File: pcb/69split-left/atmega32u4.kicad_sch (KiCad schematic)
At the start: 16 parts, among them J2 Conn_02x03_Odd_Even, SW1 SW_Push, U1 ATmega32U4-AU, Y1 Crystal

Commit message: Moved things around so it's less confusing.
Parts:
- renumbered C5 to C2, C6 to C3, C7 to C4, C8 to C5, C2 to C6, C3 to C7, C4 to C8, R8 to R6, R9 to R8, R6 to R9

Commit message: Started layout?
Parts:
- renumbered C6 to C1, C7 to C2, C8 to C3, C2 to C4, C3 to C5, C4 to C6, C5 to C7, J2 to J1, R5 to R1, R7 to R2, R6 to R3, R8 to R4, R9 to R5
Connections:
- net RESET: now also C4.1, R1.1, SW1.2, U1.13 (~{RESET})

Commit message: Continued layout.
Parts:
- removed R2, R3, R4: 330R, Resistor_SMD:R_0603_1608Metric_Pad0.98x0.95mm_HandSolder, symbol Device:R
- added C9: 1u, Capacitor_SMD:C_0603_1608Metric_Pad1.08x0.95mm_HandSolder, symbol Device:C_Small
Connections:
- net VBUS is gone; now on net VCC: U1.7 (VBUS)
- net GND: now also C9.2
- net GPIO_OUT_PB5: now also U1.29 (PB5)
- net GPIO_OUT_PB6: now also U1.30 (PB6)
- net GPIO_OUT_PB7: now also U1.12 (PB7)
- net VCC: now also C9.1
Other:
- moved on the sheet: C2

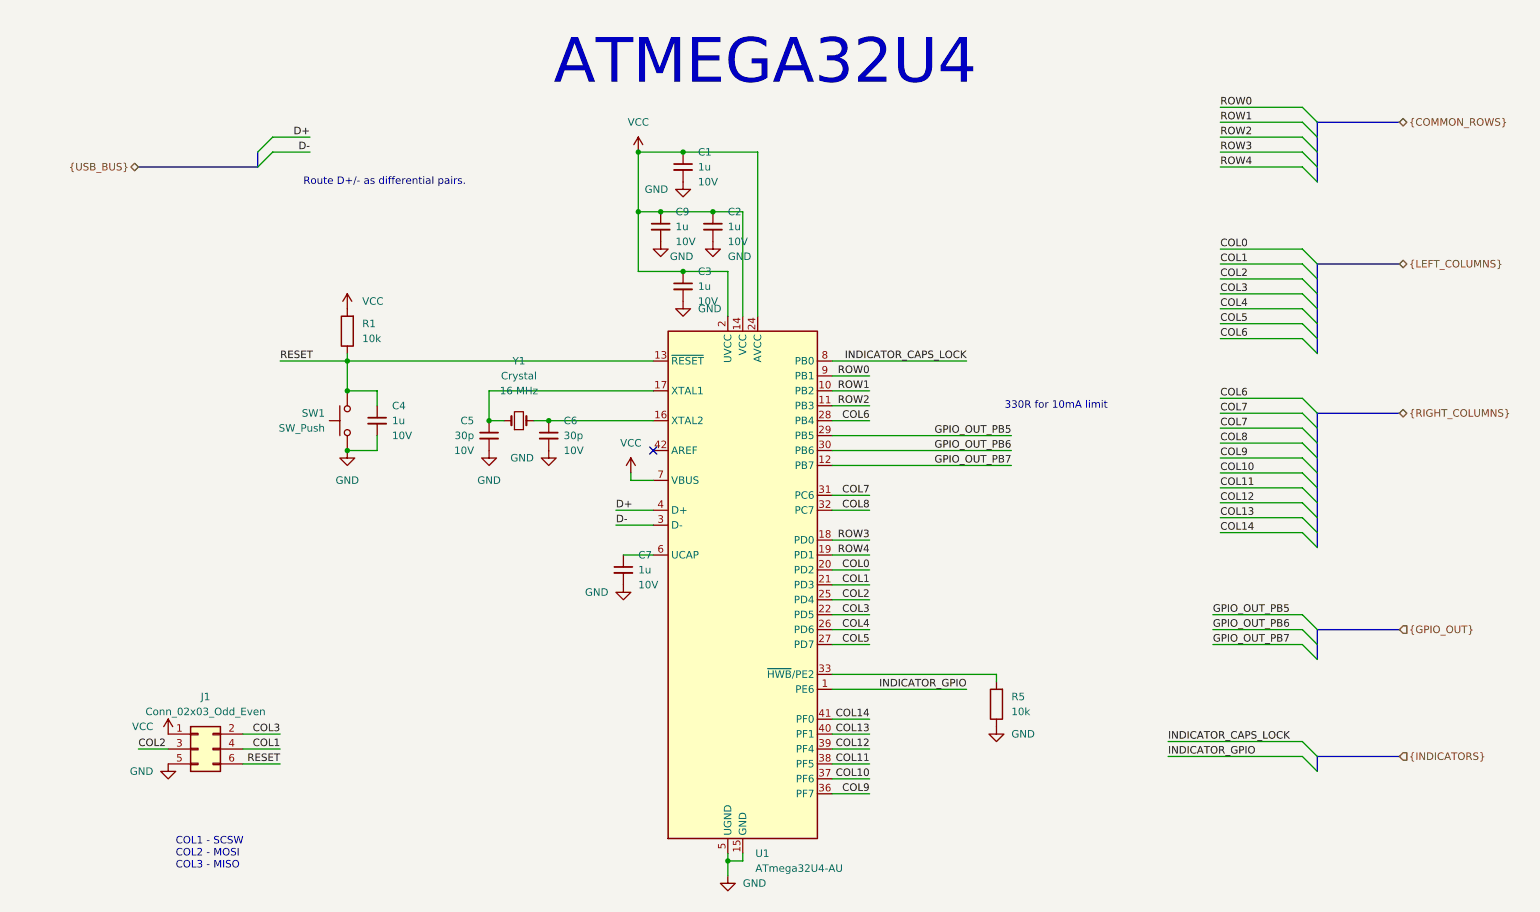
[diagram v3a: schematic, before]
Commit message: Practically finished the left side - need to make a footprint for the split USB connector. Some other schematic changes were made that I will not list. I should've made more commits between ths one and the previous one but it is what it is.
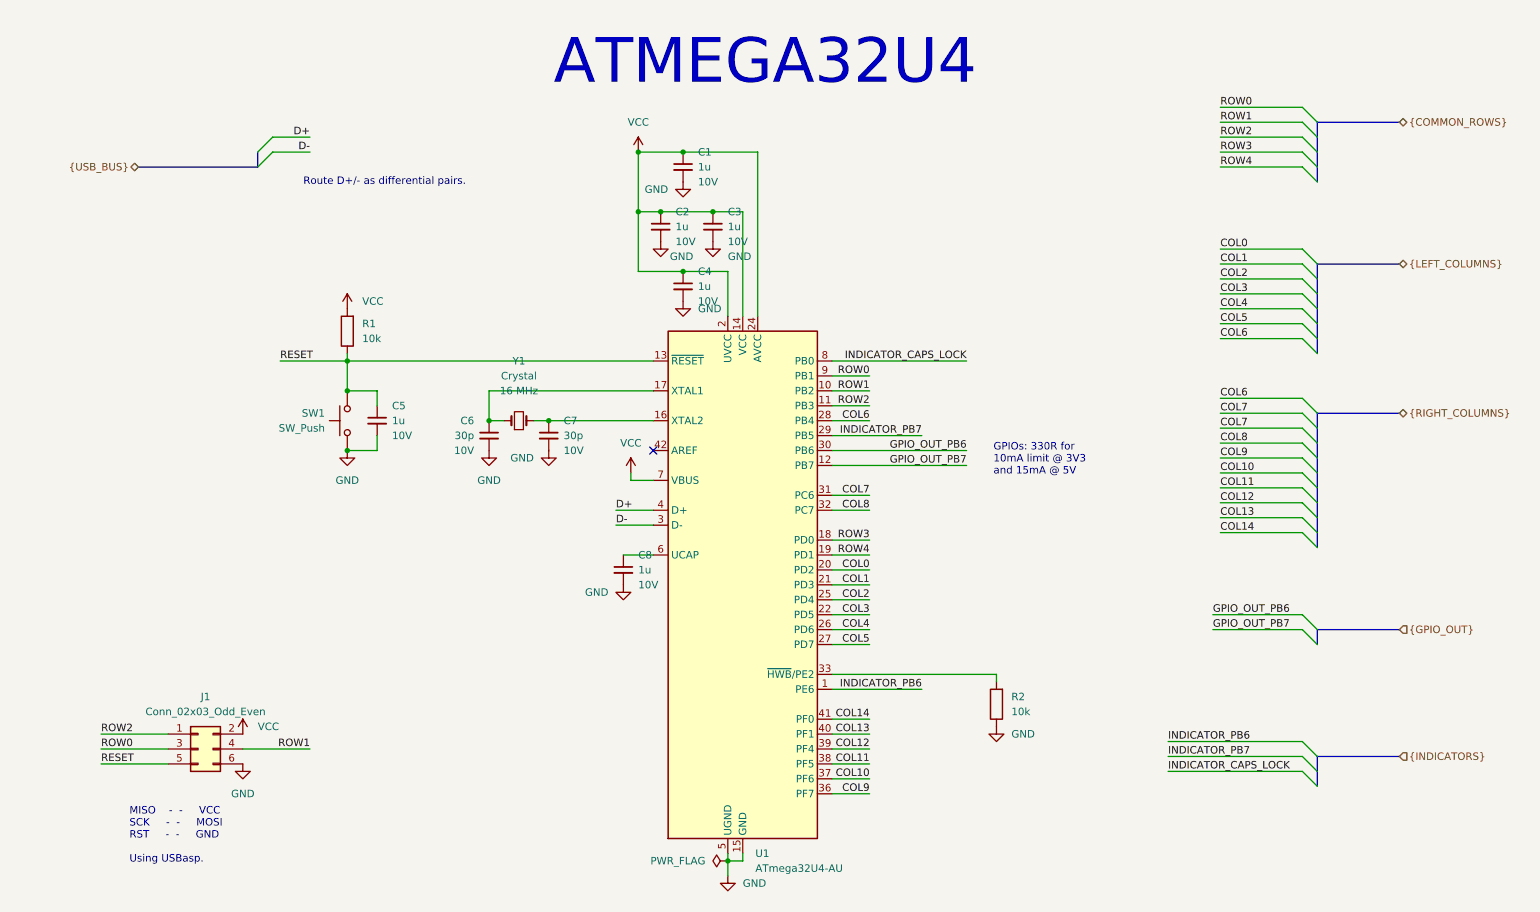
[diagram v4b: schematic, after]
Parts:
- renumbered C9 to C2, C2 to C3, C3 to C4, C4 to C5, C5 to C6, C6 to C7, C7 to C8, R5 to R2
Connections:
- net COL1: no longer J1.4 (Pin_4)
- net COL2: no longer J1.3 (Pin_3)
- net COL3: no longer J1.2 (Pin_2)
- net GND: now also J1.6 (Pin_6); no longer J1.5 (Pin_5)
- net RESET: now also J1.5 (Pin_5); no longer J1.6 (Pin_6)
- net ROW0: now also J1.3 (Pin_3)
- net ROW1: now also J1.4 (Pin_4)
- net ROW2: now also J1.1 (Pin_1)
- net VCC: now also J1.2 (Pin_2); no longer J1.1 (Pin_1)
- net GPIO_OUT_PB5 renamed INDICATOR_PB7
- net INDICATOR_GPIO renamed INDICATOR_PB6
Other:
- note added: "GPIOs: 330R for 10mA limit @ 3V3 and 15mA @ 5V"
- note added: "MISO - - VCC SCK - - MOSI RST - - GND Using USBasp."
- note removed: "330R for 10mA limit"
- note removed: "COL1 - SCSW COL2 - MOSI COL3 - MISO"

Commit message: Started changing things gain to use an I/O expander with I2C.
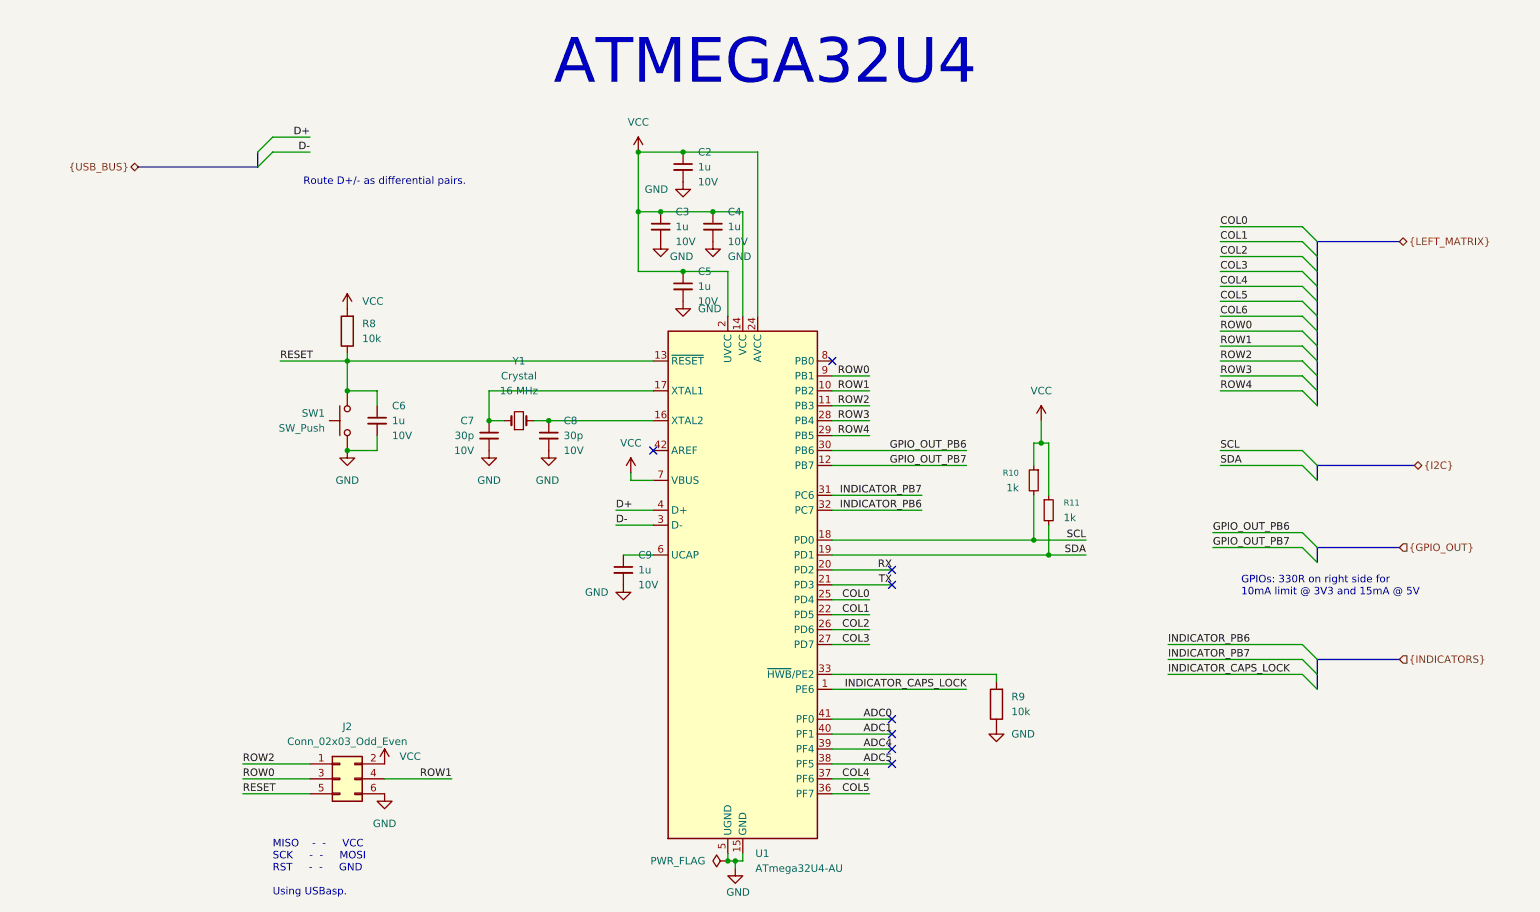
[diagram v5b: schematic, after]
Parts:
- added R10, R11: 1k, Resistor_SMD:R_0603_1608Metric_Pad0.98x0.95mm_HandSolder, symbol Device:R_Small
- renumbered C1 to C2, C2 to C3, C3 to C4, C4 to C5, C5 to C6, C6 to C7, C7 to C8, C8 to C9, J1 to J2, R1 to R8, R2 to R9
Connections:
- net COL10 is gone; now on net COL4: U1.37 (PF6)
- net COL7 is gone; now on net INDICATOR_PB7: U1.31 (PC6)
- net COL8 is gone; now on net INDICATOR_PB6: U1.32 (PC7)
- net COL9 is gone; now on net COL5: U1.36 (PF7)
- net COL0: now also U1.25 (PD4); no longer U1.20 (PD2)
- net COL1: now also U1.22 (PD5); no longer U1.21 (PD3)
- net COL2: now also U1.26 (PD6); no longer U1.25 (PD4)
- net COL3: now also U1.27 (PD7); no longer U1.22 (PD5)
- net COL4: no longer U1.26 (PD6)
- net COL5: no longer U1.27 (PD7)
- net COL6: no longer U1.28 (PB4)
- net INDICATOR_CAPS_LOCK: now also U1.1 (PE6); no longer U1.8 (PB0)
- net INDICATOR_PB6: no longer U1.1 (PE6)
- net INDICATOR_PB7: no longer U1.29 (PB5)
- net ROW3: now also U1.28 (PB4); no longer U1.18 (PD0)
- net ROW4: now also U1.29 (PB5); no longer U1.19 (PD1)
- net VCC: now also R10.1, R11.1
- net COL11 renamed ADC5
- net COL12 renamed ADC4
- net COL13 renamed ADC1
- net COL14 renamed ADC0
- new net RX: U1.20 (PD2)
- new net SCL: R10.2, U1.18 (PD0)
- new net SDA: R11.2, U1.19 (PD1)
- new net TX: U1.21 (PD3)
- no-connect marks 1 -> 8
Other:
- note added: "GPIOs: 330R on right side for 10mA limit @ 3V3 and 15mA @ 5V"
- note removed: "GPIOs: 330R for 10mA limit @ 3V3 and 15mA @ 5V"
- company: (none) -> Yiannis Michael
- title: 69SPLIT KEYBOARD -> 69SPLIT
- moved on the sheet: J2

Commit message: Finished left keyboard again...
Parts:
- R10, R11: now not fitted
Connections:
- net ADC5 is gone; now on net COL4: U1.38 (PF5)
- net COL4: no longer U1.37 (PF6)
- net COL5: now also U1.37 (PF6); no longer U1.36 (PF7)
- net COL6: now also U1.36 (PF7)
- net PB0/CS: now reaches U1.8 (PB0)
- no-connect marks 8 -> 1

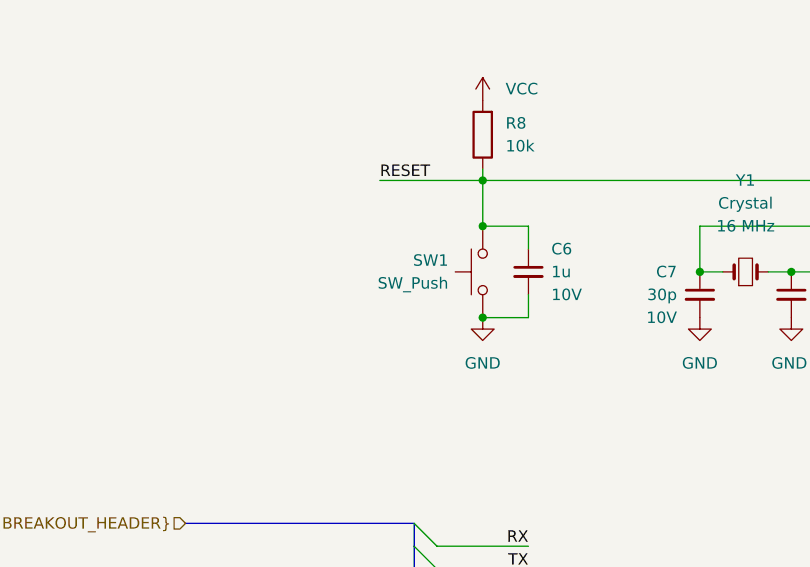
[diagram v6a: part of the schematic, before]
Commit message: Minor improvements to left schematic and layout.
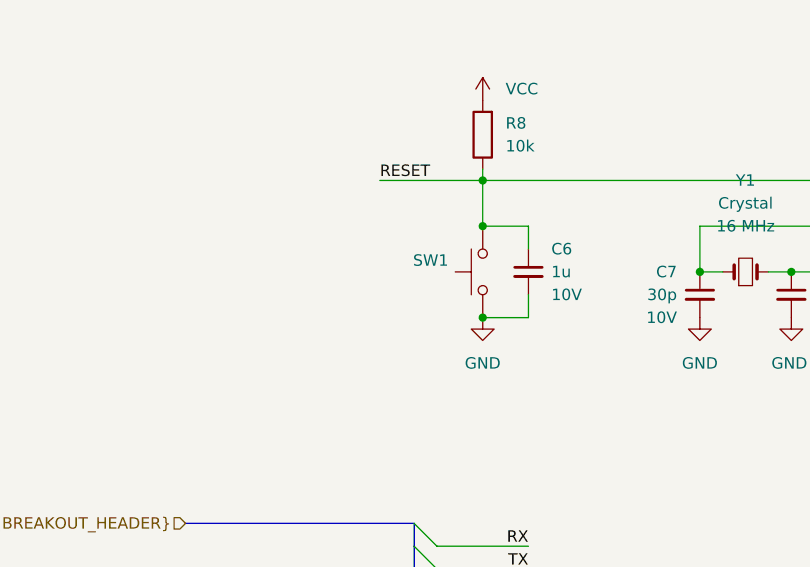
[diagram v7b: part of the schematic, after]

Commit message: Alright I think now the left side is actually ready.
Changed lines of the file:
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@@
+	)
+	(bus_entry
+		(at 67.31 133.35)
+		(size 2.54 2.54)
+		(stroke
+			(width 0)
+			(type default)
+		)
 	)
 	(bus_entry
@@
 	)
 	(bus_entry
+		(at 67.31 130.81)
+		(size 2.54 2.54)
+		(stroke
+			(width 0)
+			(type default)
+		)
+	)
+	(bus_entry
 		(at 240.03 95.25)
 		(size -2.54 -2.54)
@@
 	(wire
 		(pts
+			(xy 69.85 135.89) (xy 80.01 135.89)
+		)
+		(stroke
+			(width 0)
+			(type default)
+		)
+	)
+	(wire
+		(pts
 			(xy 124.46 41.91) (xy 124.46 52.07)
 		)
@@
 		)
 	)
+	(bus
+		(pts
+			(xy 67.31 128.27) (xy 67.31 130.81)
+		)
+		(stroke
+			(width 0)
+			(type default)
+		)
+	)
 	(wire
 		(pts
@@
 		)
 	)
+	(wire
+		(pts
+			(xy 69.85 133.35) (xy 80.01 133.35)
+		)
+		(stroke
+			(width 0)
+			(type default)
+		)
+	)
 	(bus
 		(pts
@@
 		(pts
 			(xy 142.24 161.29) (xy 142.24 162.56)
+		)
+		(stroke
+			(width 0)
+			(type default)
+		)
+	)
+	(bus
+		(pts
+			(xy 67.31 130.81) (xy 67.31 133.35)
 		)
 		(stroke
@@
 		)
 	)
+	(label "SDA"
+		(at 80.01 135.89 180)
+		(effects
+			(font
+				(size 1.27 1.27)
+			)
+			(justify right bottom)
+		)
+	)
 	(label "GPIO_OUT_PB7"
 		(at 180.34 95.25 180)
@@
 		)
 	)
+	(label "SCL"
+		(at 80.01 133.35 180)
+		(effects
+			(font
+				(size 1.27 1.27)
+			)
+			(justify right bottom)
+		)
+	)
